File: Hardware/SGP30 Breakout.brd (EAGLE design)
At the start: 25.4 x 25.4 mm, 38 parts, among them J3 PTH, U1 SGP30, U2 MIC5504

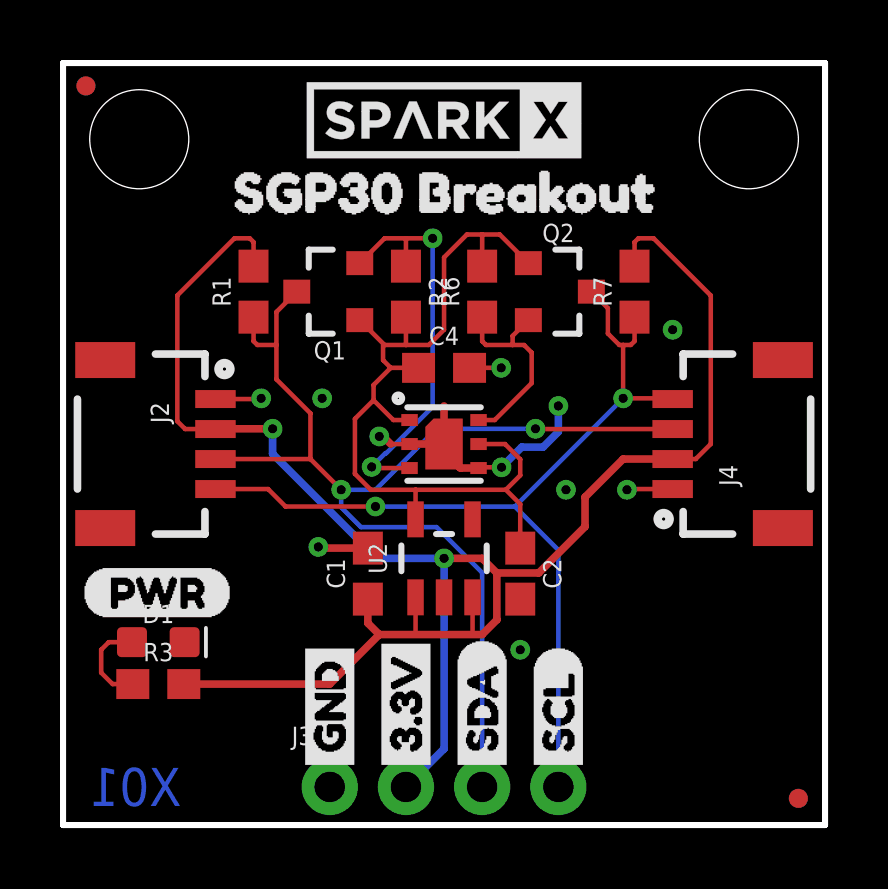
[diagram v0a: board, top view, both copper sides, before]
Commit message: fixed missing ground connection
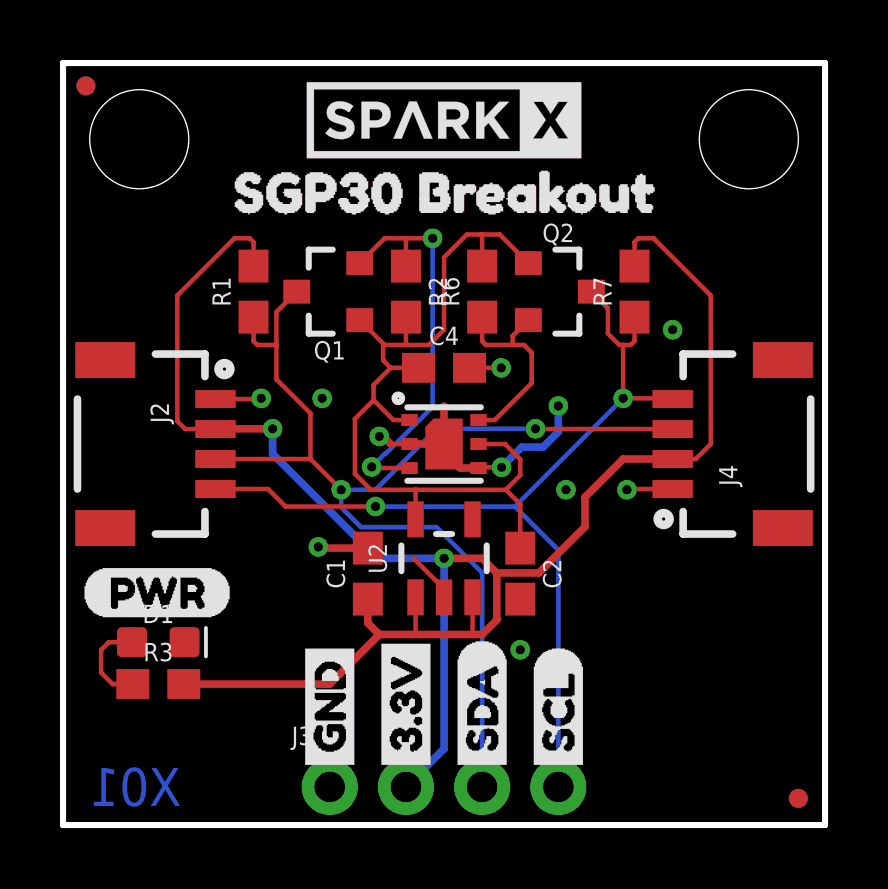
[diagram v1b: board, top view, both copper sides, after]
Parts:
- U2: value MIC5504 -> AP2112k
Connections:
- removed net N$6: U2.2
- net GND: now also U2.2
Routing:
- net GND: track 17.1 -> 18.9 mm
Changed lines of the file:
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@@
 <layer number="23" name="tOrigins" color="15" fill="1" visible="yes" active="yes"/>
 <layer number="24" name="bOrigins" color="15" fill="1" visible="yes" active="yes"/>
-<layer number="25" name="tNames" color="7" fill="1" visible="no" active="yes"/>
-<layer number="26" name="bNames" color="7" fill="1" visible="no" active="yes"/>
-<layer number="27" name="tValues" color="7" fill="1" visible="no" active="yes"/>
-<layer number="28" name="bValues" color="7" fill="1" visible="no" active="yes"/>
-<layer number="29" name="tStop" color="7" fill="3" visible="no" active="yes"/>
-<layer number="30" name="bStop" color="7" fill="6" visible="no" active="yes"/>
-<layer number="31" name="tCream" color="7" fill="4" visible="no" active="yes"/>
-<layer number="32" name="bCream" color="7" fill="5" visible="no" active="yes"/>
-<layer number="33" name="tFinish" color="6" fill="3" visible="no" active="yes"/>
-<layer number="34" name="bFinish" color="6" fill="6" visible="no" active="yes"/>
-<layer number="35" name="tGlue" color="7" fill="4" visible="no" active="yes"/>
-<layer number="36" name="bGlue" color="7" fill="5" visible="no" active="yes"/>
-<layer number="37" name="tTest" color="7" fill="1" visible="no" active="yes"/>
-<layer number="38" name="bTest" color="7" fill="1" visible="no" active="yes"/>
-<layer number="39" name="tKeepout" color="4" fill="11" visible="no" active="yes"/>
-<layer number="40" name="bKeepout" color="1" fill="11" visible="no" active="yes"/>
-<layer number="41" name="tRestrict" color="4" fill="10" visible="no" active="yes"/>
-<layer number="42" name="bRestrict" color="1" fill="10" visible="no" active="yes"/>
-<layer number="43" name="vRestrict" color="2" fill="10" visible="no" active="yes"/>
-<layer number="44" name="Drills" color="7" fill="1" visible="no" active="yes"/>
+<layer number="25" name="tNames" color="7" fill="1" visible="yes" active="yes"/>
+<layer number="26" name="bNames" color="7" fill="1" visible="yes" active="yes"/>
+<layer number="27" name="tValues" color="7" fill="1" visible="yes" active="yes"/>
+<layer number="28" name="bValues" color="7" fill="1" visible="yes" active="yes"/>
+<layer number="29" name="tStop" color="7" fill="3" visible="yes" active="yes"/>
+<layer number="30" name="bStop" color="7" fill="6" visible="yes" active="yes"/>
+<layer number="31" name="tCream" color="7" fill="4" visible="yes" active="yes"/>
+<layer number="32" name="bCream" color="7" fill="5" visible="yes" active="yes"/>
+<layer number="33" name="tFinish" color="6" fill="3" visible="yes" active="yes"/>
+<layer number="34" name="bFinish" color="6" fill="6" visible="yes" active="yes"/>
+<layer number="35" name="tGlue" color="7" fill="4" visible="yes" active="yes"/>
+<layer number="36" name="bGlue" color="7" fill="5" visible="yes" active="yes"/>
+<layer number="37" name="tTest" color="7" fill="1" visible="yes" active="yes"/>
+<layer number="38" name="bTest" color="7" fill="1" visible="yes" active="yes"/>
+<layer number="39" name="tKeepout" color="4" fill="11" visible="yes" active="yes"/>
+<layer number="40" name="bKeepout" color="1" fill="11" visible="yes" active="yes"/>
+<layer number="41" name="tRestrict" color="4" fill="10" visible="yes" active="yes"/>
+<layer number="42" name="bRestrict" color="1" fill="10" visible="yes" active="yes"/>
+<layer number="43" name="vRestrict" color="2" fill="10" visible="yes" active="yes"/>
+<layer number="44" name="Drills" color="7" fill="1" visible="yes" active="yes"/>
 <layer number="45" name="Holes" color="7" fill="1" visible="yes" active="yes"/>
 <layer number="46" name="Milling" color="3" fill="1" visible="yes" active="yes"/>
 <layer number="47" name="Measures" color="7" fill="1" visible="yes" active="yes"/>
-<layer number="48" name="Document" color="7" fill="1" visible="no" active="yes"/>
-<layer number="49" name="Reference" color="7" fill="1" visible="no" active="yes"/>
-<layer number="50" name="dxf" color="7" fill="1" visible="no" active="yes"/>
+<layer number="48" name="Document" color="7" fill="1" visible="yes" active="yes"/>
+<layer number="49" name="Reference" color="7" fill="1" visible="yes" active="yes"/>
+<layer number="50" name="dxf" color="7" fill="1" visible="yes" active="yes"/>
 <layer number="51" name="tDocu" color="6" fill="1" visible="yes" active="yes"/>
-<layer number="52" name="bDocu" color="7" fill="1" visible="no" active="yes"/>
+<layer number="52" name="bDocu" color="7" fill="1" visible="yes" active="yes"/>
 <layer number="91" name="Nets" color="2" fill="1" visible="no" active="no"/>
 <layer number="92" name="Busses" color="1" fill="1" visible="no" active="no"/>
@@
 <element name="U$29" library="Labels" package="QWIIC-LOGO-MEDIUM" value="" x="21.59" y="4.318" rot="MR0"/>
 <element name="U1" library="SGP30" package="SGP30" value="SGP30" x="12.7" y="12.7"/>
-<element name="U2" library="SGP30" package="SOT23-5" value="MIC5504" x="12.7" y="8.89"/>
+<element name="U2" library="SGP30" package="SOT23-5" value="AP2112k" x="12.7" y="8.89"/>
 <element name="Q1" library="SparkFun-DiscreteSemi" package="SOT23-3" value="" x="8.89" y="17.78" rot="R90">
 <attribute name="PROD_ID" value="TRANS-00830" x="8.89" y="17.78" size="1.778" layer="27" font="vector" ratio="15" rot="R90" display="off"/>
@@
 <wire x1="12.7" y1="2.54" x2="12.7" y2="8.89" width="0.254" layer="16"/>
 </signal>
-<signal name="GND" airwireshidden="yes">
+<signal name="GND">
 <polygon width="0.254" layer="16" isolate="0.3048">
 <vertex x="0" y="0"/>
@@
 <wire x1="12.573" y1="12.573" x2="12.573" y2="12.7" width="0.254" layer="1"/>
 <wire x1="12.7" y1="12.7" x2="12.7" y2="13.97" width="0.254" layer="1"/>
+<contactref element="U2" pad="2"/>
+<wire x1="12.7" y1="7.5899" x2="12.7" y2="7.874" width="0.1524" layer="1"/>
+<wire x1="12.7" y1="7.874" x2="11.684" y2="8.89" width="0.1524" layer="1"/>
 </signal>
 <signal name="SCL">
@@
 <wire x1="10.718" y1="16.002" x2="11.43" y2="16.002" width="0.1524" layer="1"/>
 </signal>
-<signal name="N$6">
-<contactref element="U2" pad="2"/>
-</signal>
 <signal name="LSDA">
 <contactref element="U1" pad="3"/>
@@
 </signal>
 </signals>
+<errors>
+</errors>
 </board>
 </drawing>

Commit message: Update Hardware/SGP30 Breakout.brd
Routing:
- net GND: track 18.9 -> 20.5 mm

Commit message: Fixed ground connections
* Pad not grounded
* Connected pad to solde mask
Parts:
- removed U$29: (no value), Labels:QWIIC-LOGO-MEDIUM
- added U$9: QWIIC_LOGO_7MM, SparkFun-Aesthetics:QWIIC_7MM
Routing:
- net 3.3V: track 68.5 -> 71.7 mm
- net GND: vias 11 -> 12
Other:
- board text added: "X02"
- board text removed: "X01"
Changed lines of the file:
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@@
 <?xml version="1.0" encoding="utf-8"?>
 <!DOCTYPE eagle SYSTEM "eagle.dtd">
-<eagle version="9.2.1">
+<eagle version="9.3.0">
 <drawing>
 <settings>
@@
 <wire x1="25.4" y1="25.4" x2="25.4" y2="0" width="0.2032" layer="20"/>
 <wire x1="25.4" y1="0" x2="0" y2="0" width="0.2032" layer="20"/>
-<text x="2.413" y="1.27" size="1.27" layer="16" font="vector" ratio="15" rot="MR0" align="center">X01</text>
+<text x="2.413" y="1.27" size="1.27" layer="16" font="vector" ratio="15" rot="MR0" align="center">X02</text>
 <dimension x1="0" y1="0" x2="0" y2="25.4" x3="-5.08" y3="12.7" textsize="1.778" textratio="15" layer="47" unit="inch"/>
 <dimension x1="2.54" y1="22.86" x2="2.54" y2="0" x3="-1.27" y3="11.43" textsize="1.778" textratio="15" layer="47" unit="inch"/>
@@
 </element>
 <element name="U$10" library="Labels-0_04" package="(PWR)" value="" x="0.635" y="7.747" smashed="yes"/>
-<element name="U$29" library="Labels" package="QWIIC-LOGO-MEDIUM" value="" x="21.59" y="4.318" smashed="yes" rot="MR0"/>
 <element name="U1" library="SGP30" package="SGP30" value="SGP30" x="12.7" y="12.7" smashed="yes"/>
 <element name="U2" library="SGP30" package="SOT23-5" value="AP2112k" x="12.7" y="8.89" smashed="yes">
@@
 <attribute name="VALUE" x="14.478" y="8.382" size="0.6096" layer="27" font="vector" ratio="20" rot="R270" align="top-center"/>
 </element>
+<element name="U$9" library="SparkFun-Aesthetics" package="QWIIC_7MM" value="QWIIC_LOGO_7MM" x="12.7" y="18.415" smashed="yes" rot="MR0"/>
 </elements>
 <signals>
@@
 <via x="6.985" y="13.208" extent="1-16" drill="0.3048"/>
 <via x="12.7" y="8.89" extent="1-16" drill="0.3048"/>
-<wire x1="11.684" y1="6.35" x2="13.65" y2="6.35" width="0.1524" layer="1"/>
-<wire x1="13.65" y1="6.35" x2="13.97" y2="6.35" width="0.1524" layer="1"/>
-<wire x1="13.65" y1="7.5899" x2="13.65" y2="6.35" width="0.1524" layer="1"/>
 <wire x1="20.193" y1="12.2" x2="20.32" y2="12.2" width="0.1524" layer="1"/>
 <contactref element="R7" pad="2"/>
@@
 <wire x1="21.59" y1="17.653" x2="19.685" y2="19.558" width="0.1524" layer="1"/>
 <contactref element="C1" pad="1"/>
-<wire x1="10.541" y1="6.35" x2="11.684" y2="6.35" width="0.1524" layer="1"/>
-<wire x1="11.75" y1="6.416" x2="11.684" y2="6.35" width="0.1524" layer="1"/>
-<wire x1="11.75" y1="7.5899" x2="11.75" y2="6.416" width="0.1524" layer="1"/>
 <wire x1="5.08" y1="13.2" x2="5.088" y2="13.208" width="0.254" layer="1"/>
 <wire x1="5.088" y1="13.208" x2="6.985" y2="13.208" width="0.254" layer="1"/>
@@
 <wire x1="18.669" y1="12.2" x2="20.193" y2="12.2" width="0.254" layer="1"/>
 <wire x1="17.399" y1="10.93" x2="18.669" y2="12.2" width="0.254" layer="1"/>
-<wire x1="4.025" y1="4.699" x2="8.89" y2="4.699" width="0.254" layer="1"/>
-<wire x1="10.16" y1="7.532" x2="10.16" y2="6.731" width="0.254" layer="1"/>
-<wire x1="10.16" y1="6.731" x2="10.541" y2="6.35" width="0.254" layer="1"/>
-<wire x1="10.541" y1="6.35" x2="13.97" y2="6.35" width="0.254" layer="1"/>
-<wire x1="14.4606" y1="6.8406" x2="13.97" y2="6.35" width="0.254" layer="1"/>
-<wire x1="14.4606" y1="8.3994" x2="14.4606" y2="6.8406" width="0.254" layer="1"/>
+<wire x1="10.16" y1="4.699" x2="4.025" y2="4.699" width="0.254" layer="1"/>
 <wire x1="14.4574" y1="8.4026" x2="14.4606" y2="8.3994" width="0.254" layer="1"/>
 <wire x1="13.97" y1="8.89" x2="14.4574" y2="8.4026" width="0.254" layer="1"/>
 <wire x1="14.4574" y1="8.4026" x2="15.85573125" y2="8.4026" width="0.254" layer="1"/>
-<wire x1="8.89" y1="4.699" x2="10.541" y2="6.35" width="0.254" layer="1"/>
 <wire x1="6.985" y1="12.37415625" x2="6.985" y2="13.208" width="0.254" layer="16"/>
 <wire x1="10.46915625" y1="8.89" x2="6.985" y2="12.37415625" width="0.254" layer="16"/>
-<wire x1="11.43" y1="1.27" x2="12.7" y2="2.54" width="0.254" layer="16"/>
-<wire x1="12.7" y1="2.54" x2="12.7" y2="8.89" width="0.254" layer="16"/>
+<wire x1="11.43" y1="1.27" x2="13.462" y2="3.302" width="0.254" layer="16"/>
+<wire x1="13.462" y1="8.128" x2="12.7" y2="8.89" width="0.254" layer="16"/>
+<wire x1="13.462" y1="8.128" x2="13.462" y2="3.302" width="0.254" layer="16"/>
+<wire x1="14.4606" y1="8.3994" x2="14.4606" y2="4.9356" width="0.254" layer="1"/>
+<wire x1="14.224" y1="4.699" x2="13.589" y2="4.699" width="0.254" layer="1"/>
+<wire x1="13.589" y1="4.699" x2="11.811" y2="4.699" width="0.254" layer="1"/>
+<wire x1="11.811" y1="4.699" x2="10.16" y2="4.699" width="0.254" layer="1"/>
+<wire x1="14.4606" y1="4.9356" x2="14.224" y2="4.699" width="0.254" layer="1"/>
+<wire x1="10.16" y1="7.532" x2="10.16" y2="4.699" width="0.1524" layer="1"/>
+<wire x1="11.75" y1="7.5899" x2="11.75" y2="4.76" width="0.1524" layer="1"/>
+<wire x1="11.75" y1="4.76" x2="11.811" y2="4.699" width="0.1524" layer="1"/>
+<wire x1="13.65" y1="4.76" x2="13.589" y2="4.699" width="0.1524" layer="1"/>
+<wire x1="13.65" y1="7.5899" x2="13.65" y2="4.76" width="0.1524" layer="1"/>
 </signal>
 <signal name="GND">
@@
 <wire x1="11.342" y1="9.232" x2="10.16" y2="9.232" width="0.1524" layer="1"/>
 <wire x1="12.7" y1="7.874" x2="11.342" y2="9.232" width="0.1524" layer="1"/>
+<via x="12.7" y="5.842" extent="1-16" drill="0.3048"/>
 </signal>
 <signal name="SCL">
